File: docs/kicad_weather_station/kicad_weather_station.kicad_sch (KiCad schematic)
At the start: 3 parts, among them U1 DHT11

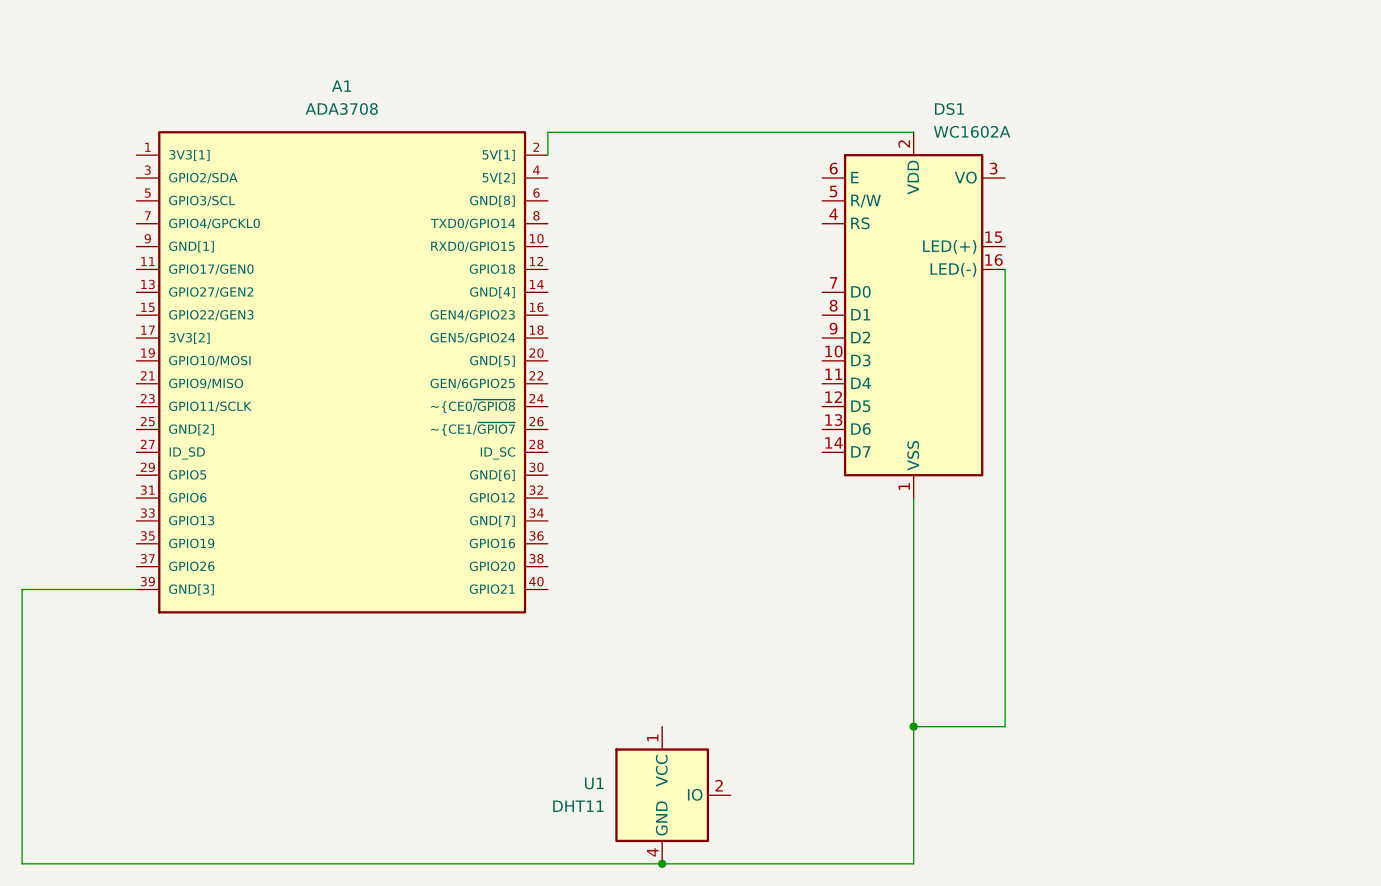
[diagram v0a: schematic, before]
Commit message: Updated README.md and schematics
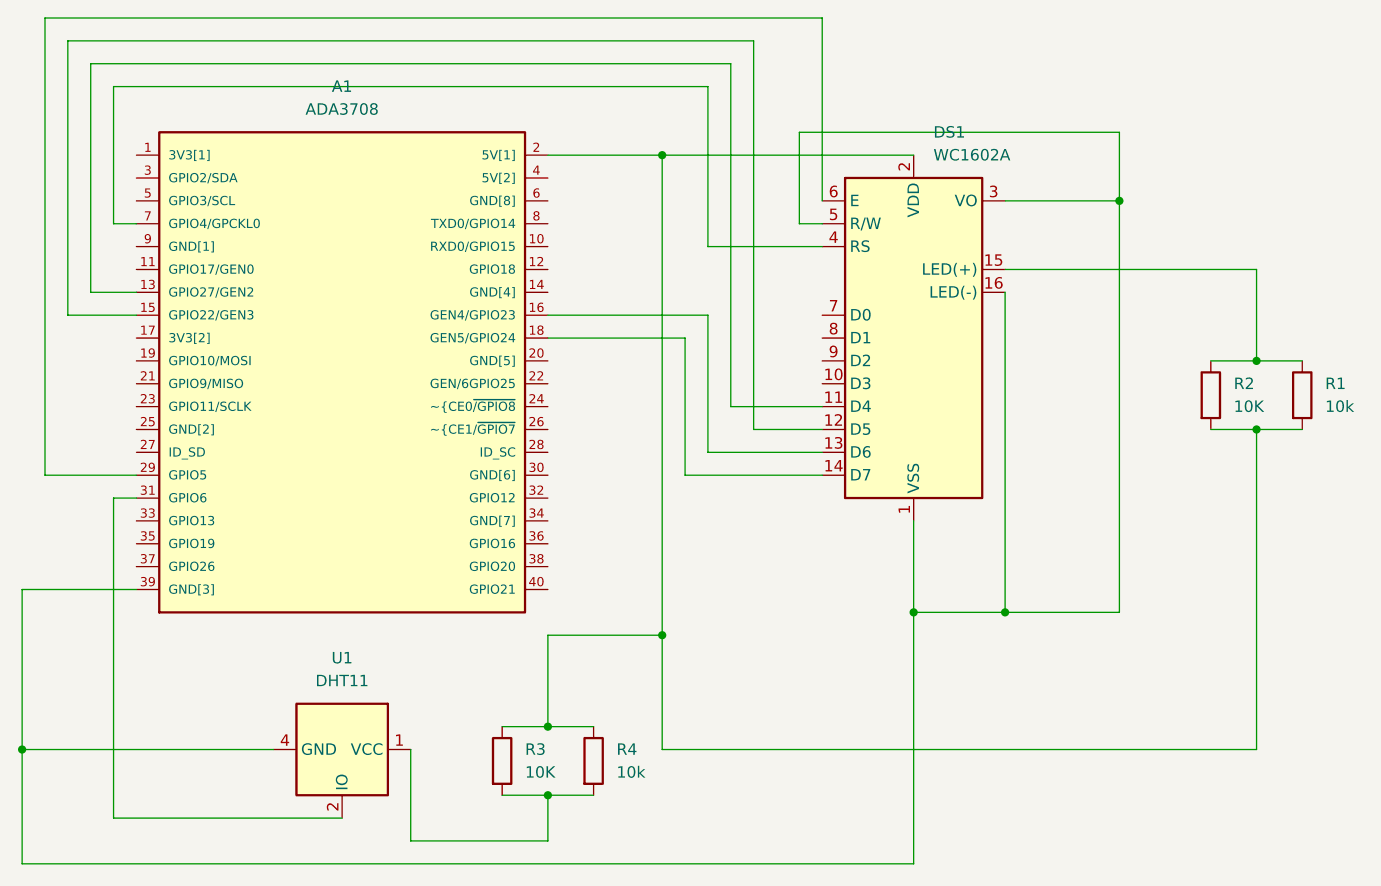
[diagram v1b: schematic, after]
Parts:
- added R1, R4: 10k, Resistor_SMD:R_0402_1005Metric, symbol Device:R
- added R2, R3: 10K, Resistor_SMD:R_0402_1005Metric, symbol Device:R
- DS1: footprint TextBasedDisplay:WC1602A -> Display:WC1602A
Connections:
- net at A1.39 (GND[3]), DS1.1 (VSS), DS1.16 (LED(-))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: now also DS1.3 (VO), DS1.5 (R/W)
- net at DS1.11 (D4): now also A1.13 (GPIO27/GEN2)
- net at DS1.12 (D5): now also A1.15 (GPIO22/GEN3)
- net at DS1.13 (D6): now also A1.16 (GEN4/GPIO23)
- net at DS1.14 (D7): now also A1.18 (GEN5/GPIO24)
- net at DS1.15 (LED(+)): now also R1.1, R2.1
- net at A1.2 (5V[1]), DS1.2 (VDD): now also R1.2, R2.2, R3.1, R4.1
- net at DS1.4 (RS): now also A1.7 (GPIO4/GPCKL0)
- net at DS1.6 (E): now also A1.29 (GPIO5)
- net at U1.1 (VCC): now also R3.2, R4.2
- net at U1.2 (IO): now also A1.31 (GPIO6)
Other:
- moved on the sheet: DS1, U1
